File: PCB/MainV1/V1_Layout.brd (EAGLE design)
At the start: 160 x 100 mm, 48 parts, among them IC1 AD826N, IC3 AD623R, U2 MB85RC256VPF-G-JNERE2, X1 STEREOJACK

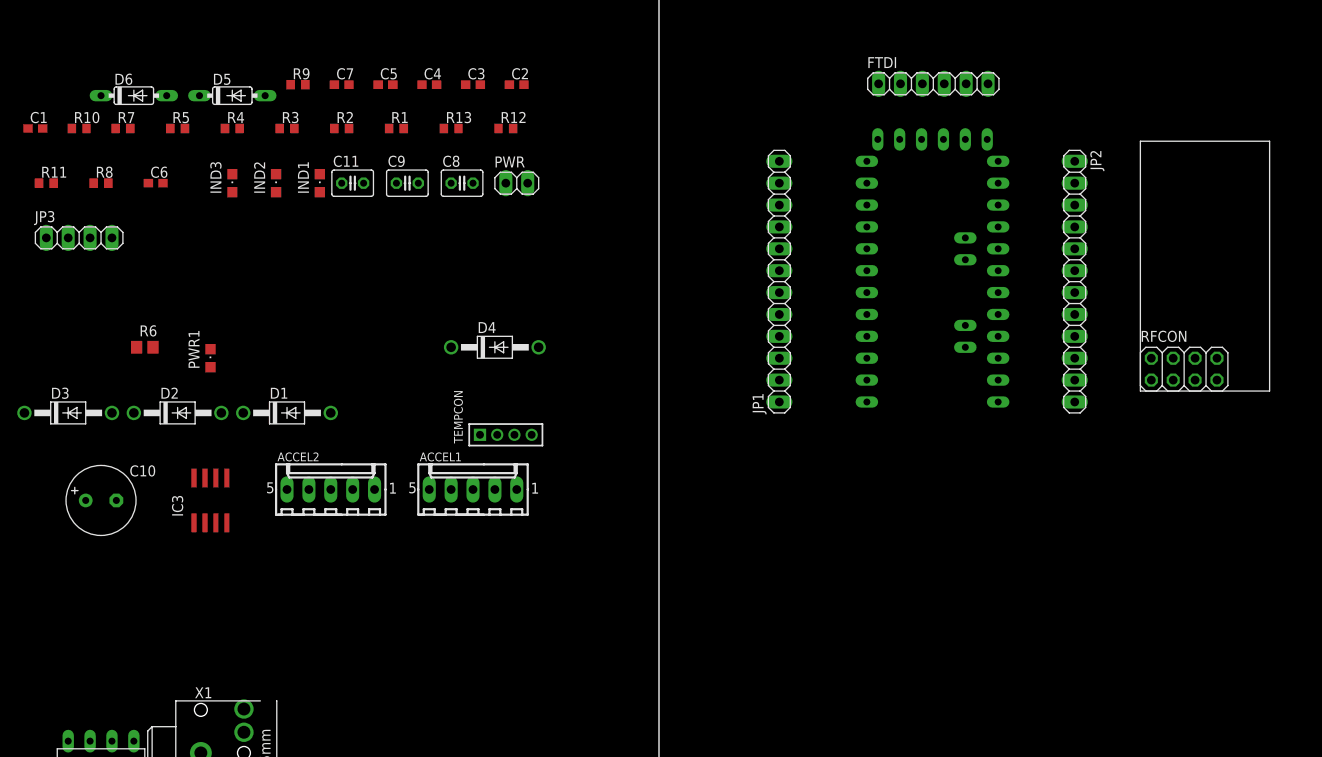
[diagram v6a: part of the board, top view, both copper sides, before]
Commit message: started initial main layout. Cleaned up files.
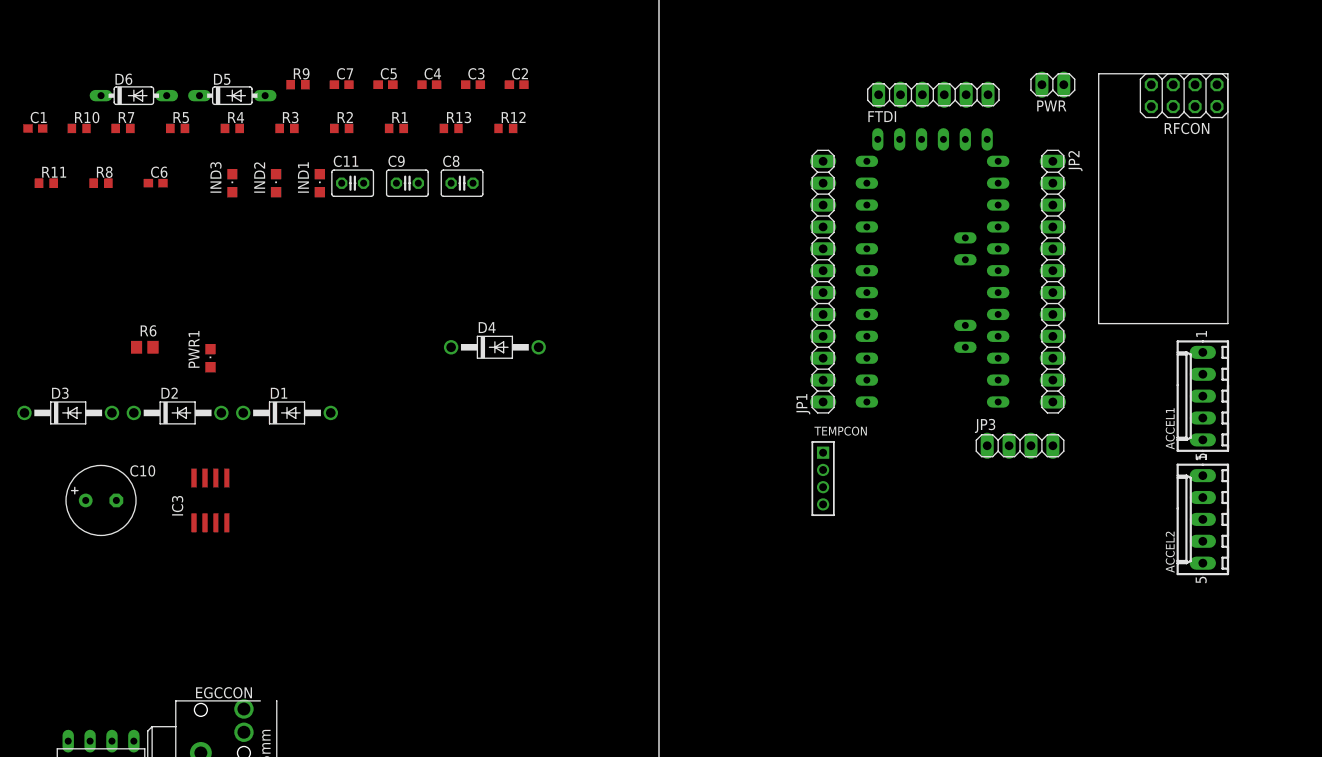
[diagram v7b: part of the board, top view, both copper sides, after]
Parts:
- moved JP3 111.9 mm to (41.9, 44.5)
- moved ACCEL2 101.3 mm to (63.1, 35.9), turned to 90 degrees
- moved ACCEL1 85.4 mm to (63.1, 50.2), turned to 90 degrees
- moved PWR 63.3 mm to (45.7, 86.4), turned to 180 degrees
- moved RFCON 38.2 mm to (66.0, 87.6), turned to 180 degrees
- moved TEMPCON 37.2 mm to (19.1, 40.6), turned to 270 degrees
- moved JP1 5.08 mm to (19.1, 63.5)
- moved JP2 2.54 mm to (45.7, 63.5)
- moved FTDI 1.27 mm to (31.8, 85.2)
- renumbered X1 to EGCCON
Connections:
- removed net N$17: JP1.8, U$1.D2
- removed net N$29: JP3.3, U$1.A7
- new net A7: C3.2, D5.C, D6.A, JP3.3, R7.2, U$1.A7
- new net D2: IND3.A, JP1.8, U$1.D2
- net A0: no longer C3.2, D5.C, D6.A, R7.2
- net D5: no longer IND3.A

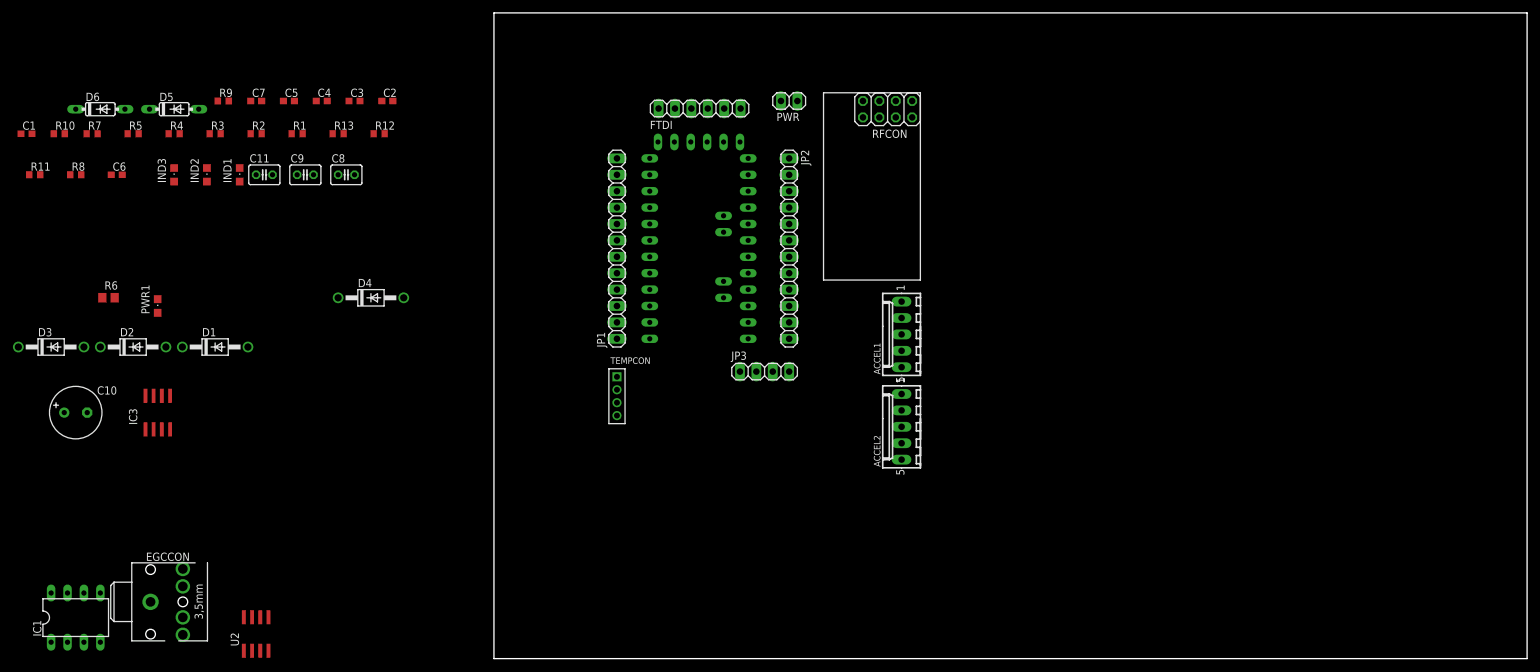
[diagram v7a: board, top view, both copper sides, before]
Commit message: First draft of completed layout and route
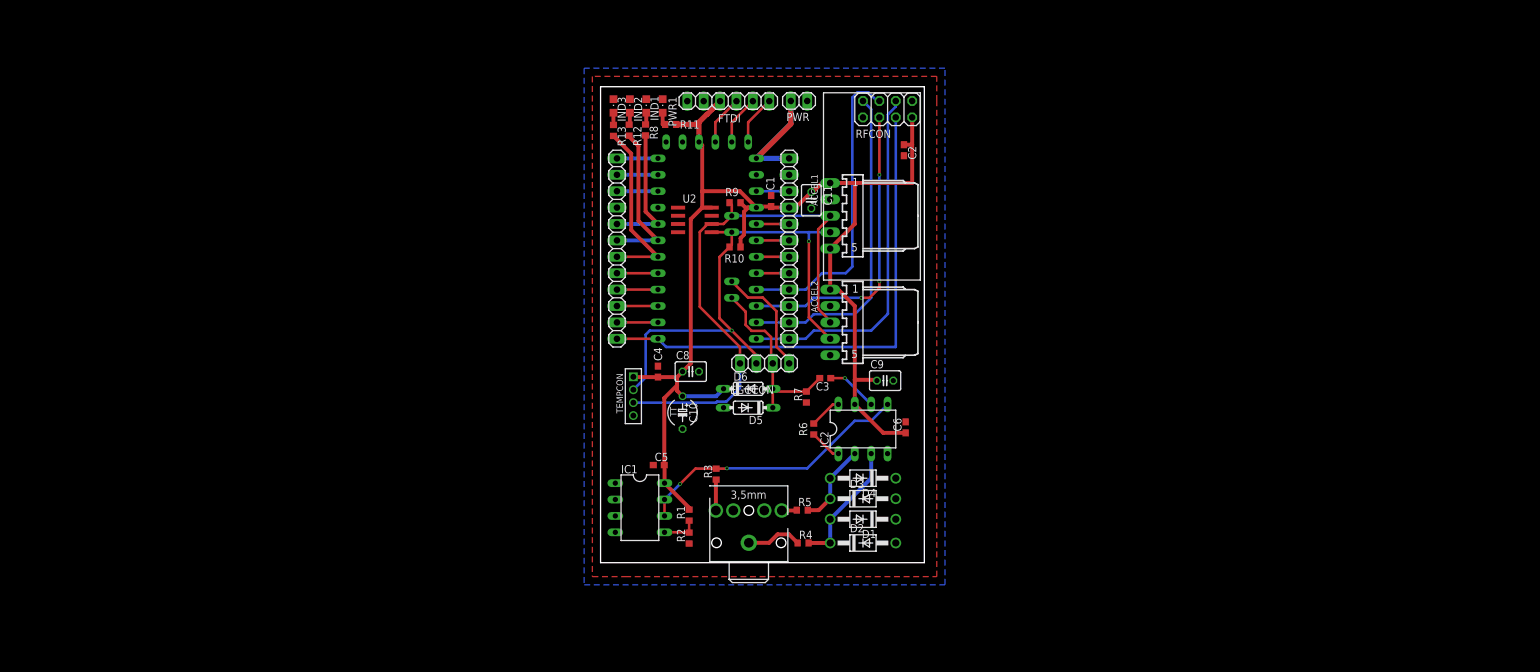
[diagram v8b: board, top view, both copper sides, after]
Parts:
- removed C7: 10nF, rcl:C0603
- removed IC3: AD623R, analog-devices:SO8
- added IC2: AD623N, analog-devices:DIL08
- ACCEL1, ACCEL2: value 22-27-2051-05 -> 22-05-7058-05; device con-molex:6410-05 -> con-molex:7395-05
- C10: device rcl:E3,5-8 -> rcl:TAP5-45
- IC1: value AD826N -> LM6482
- R6: device rcl:R0805 -> rcl:R0603
- moved C6 128.3 mm to (63.8, 35.8), turned to 90 degrees
- moved D3 127.9 mm to (57.1, 24.8)
- moved R5 118.9 mm to (47.8, 23.0)
- moved R7 117.9 mm to (48.4, 40.5), turned to 90 degrees
- moved D2 117.0 mm to (57.1, 17.9)
- moved R4 116.2 mm to (47.9, 17.9)
- moved C1 115.8 mm to (42.9, 70.9), turned to 90 degrees
- moved R6 111.1 mm to (49.5, 35.6), turned to 270 degrees
- moved D6 109.3 mm to (39.4, 41.8)
- moved R10 106.1 mm to (37.3, 63.8)
- moved D1 103.8 mm to (57.1, 21.6), turned to 180 degrees
- moved D5 100.2 mm to (39.4, 38.9), turned to 180 degrees
- moved R11 98.8 mm to (27.4, 82.7)
- moved EGCCON 95.5 mm to (39.4, 15.2), turned to 90 degrees
- moved C9 95.3 mm to (60.6, 43.1)
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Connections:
- removed net A7: C3.2, D5.C, D6.A, JP3.3, R7.2, U$1.A7
- new net A6: C3.2, D5.C, D6.A, JP3.3, R7.2, U$1.A6
- net +3V3: now also IC2.7, R11.2; no longer C7.1, IC3.7, PWR1.A
- net AGND: now also IC1.6, IC1.7, IC2.5; no longer IC1.1, IC1.2, IC3.5
- net D2: now also R8.2; no longer IND3.A
- net D3: now also R12.2; no longer IND1.A
- net D4: now also R13.2; no longer IND2.A
- net GND: now also IC1.2, IC1.3, IC2.4, IND1.C, IND2.C, IND3.C, PWR1.C; no longer C7.2, IC1.5, IC1.6, IC3.4, R11.1, R12.1, R13.1, R8.1
- net N$1: now also PWR1.A, R11.1; no longer PWR1.C, R11.2
- net N$14: now also IND1.A, R8.1; no longer IND1.C, R8.2
- net N$15: now also IND2.A, R12.1; no longer IND2.C, R12.2
- net N$16: now also IND3.A, R13.1; no longer IND3.C, R13.2
- net N$2: now also IC2.2; no longer IC3.2
- net N$28: now also U$1.A7; no longer U$1.A6
- net N$3: now also IC1.5; no longer IC1.3
- net N$5: now also IC2.3; no longer IC3.3
- net N$6: now also IC2.6; no longer IC3.6
- net N$7: now also IC2.8, R6.1; no longer IC3.8, R6.2
- net N$8: now also IC2.1, R6.2; no longer IC3.1, R6.1
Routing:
- net +3V3: track 0.00 -> 197.1 mm
- net SCL: track 0.00 -> 85.6 mm
- net SDA: track 0.00 -> 82.6 mm, vias 0 -> 2
- net D9: track 0.00 -> 79.3 mm
- net D10: track 0.00 -> 55.4 mm
- net D11: track 0.00 -> 50.4 mm
- net D13: track 0.00 -> 47.6 mm
- net D12: track 0.00 -> 46.6 mm, vias 0 -> 3
- net AGND: track 0.00 -> 43.2 mm, vias 0 -> 2
- net A6: track 0.00 -> 29.2 mm
- net D4: track 0.00 -> 27.9 mm
- net N$21: track 0.00 -> 27.3 mm
- net D3: track 0.00 -> 24.4 mm
- net D2: track 0.00 -> 20.9 mm
- net N$5: track 0.00 -> 19.8 mm
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- added copper zone on layer 1, net GND
- added copper zone on layer 16, net GND
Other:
- board size 160 x 100 mm -> 50.1 x 73.7 mm
